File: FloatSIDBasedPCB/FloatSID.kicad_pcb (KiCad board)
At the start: 2 copper layers, 18 parts, among them M1 Motor_DC, SW1 SW, SW2 Limit Switch, U2 MS583730BA01-50, U4 XiaoESP32C3

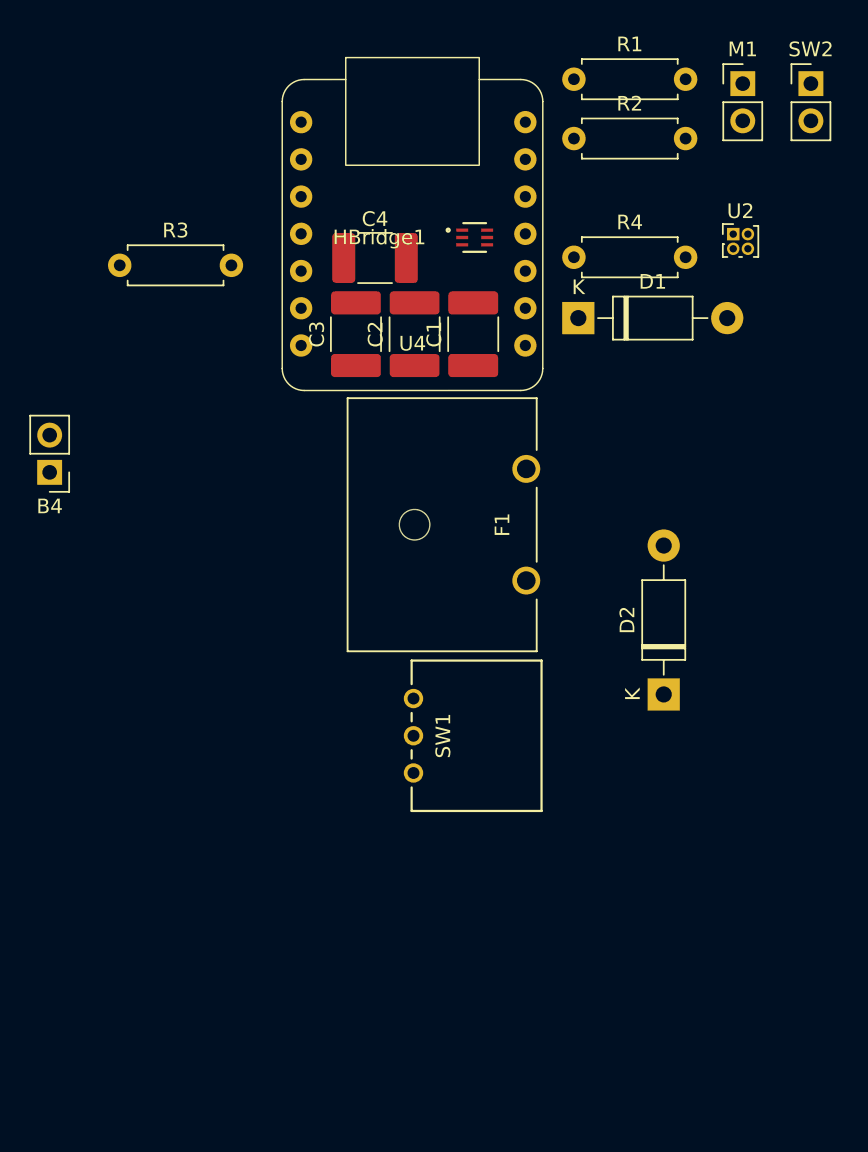
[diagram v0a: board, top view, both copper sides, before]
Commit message: Added Preliminary Traces for PCB
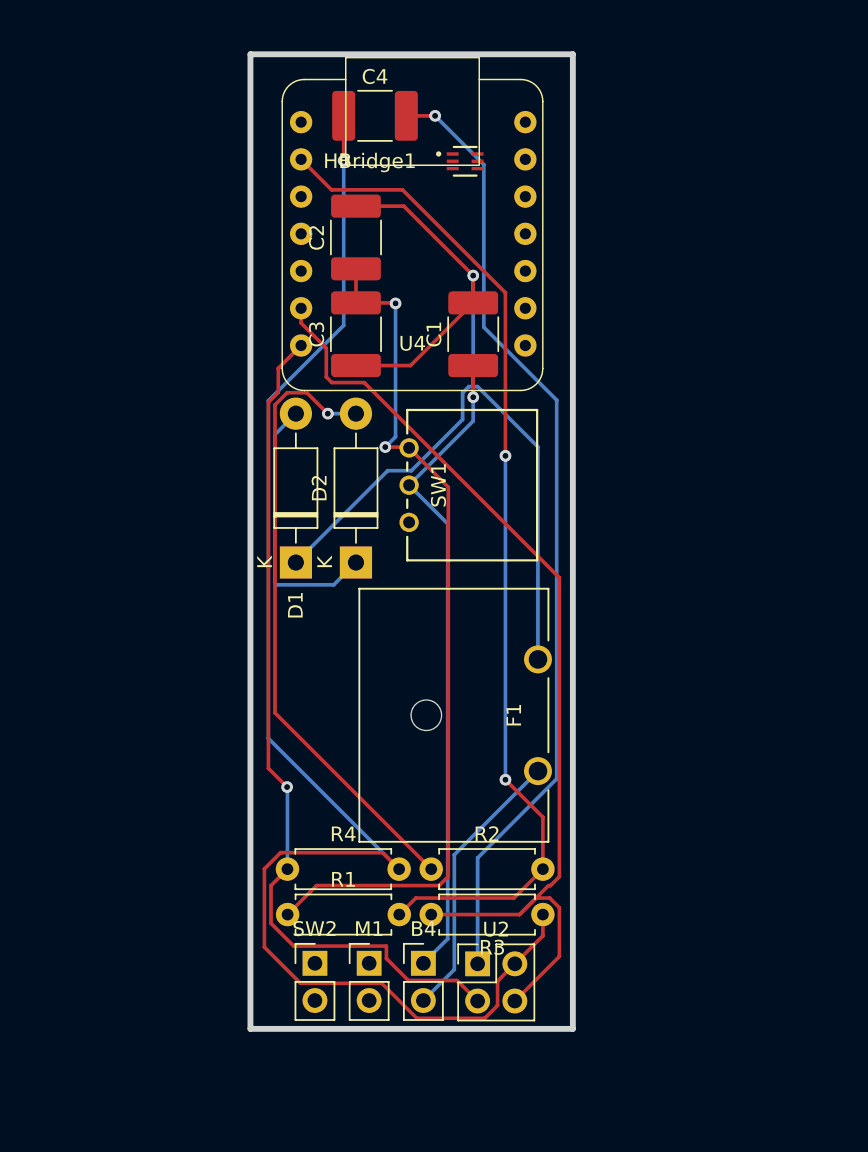
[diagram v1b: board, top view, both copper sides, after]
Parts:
- U2: footprint Connector_PinHeader_1.00mm:PinHeader_2x02_P1.00mm_Vertical -> Connector_PinHeader_2.54mm:PinHeader_2x02_P2.54mm_Vertical
- moved SW2 68.9 mm to (118.9, 135.2)
- moved M1 65.2 mm to (122.6, 135.2)
- moved R1 60.3 mm to (117.0, 131.9)
- moved R3 52.9 mm to (134.5, 131.9), turned to 180 degrees
- moved U2 52.8 mm to (130.0, 135.3)
- moved R2 50.8 mm to (126.8, 128.8)
- moved R4 46.1 mm to (117.0, 128.8)
- moved B4 42.1 mm to (126.3, 135.2), turned to 0 degrees
- moved D1 25.5 mm to (117.6, 107.9), turned to 90 degrees
- moved D2 22.8 mm to (121.7, 107.9)
- moved SW1 17.1 mm to (125.3, 102.6)
- moved F1 13.0 mm to (126.5, 118.3)
- moved C4 9.70 mm to (123.0, 77.4)
- moved C2 7.72 mm to (121.7, 85.7)
- moved HBridge1 5.24 mm to (129.1, 80.5)
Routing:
- net Net-(U2-VDD): track 0.00 -> 98.5 mm, vias 0 -> 1
- net Net-(U4-D0): track 0.00 -> 69.2 mm, vias 0 -> 2
- net Net-(U2-SDA): track 0.00 -> 68.3 mm
- net Net-(D1-K): track 0.00 -> 67.9 mm, vias 0 -> 1
- net Net-(U2-GND): track 0.00 -> 65.5 mm, vias 0 -> 1
- net Net-(HBridge1-VDD): track 0.00 -> 59.2 mm, vias 0 -> 2
- net Net-(U2-SCL): track 0.00 -> 58.2 mm, vias 0 -> 1
- net Net-(B4-+): track 0.00 -> 44.4 mm, vias 0 -> 1
- net Net-(D2-A): track 0.00 -> 43.4 mm, vias 0 -> 1
- net Net-(B4--): track 0.00 -> 18.9 mm
- net Net-(D1-A): track 0.00 -> 18.4 mm
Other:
- board outline added: 22 x 66.5 mm

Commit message: Updated PCB
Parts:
- moved H1 2.16 mm to (129.6, 82.6)
- moved C1 0.60 mm to (129.1, 92.3)
- renumbered HBridge1 to H1
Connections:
- H1 pad 1: (no net) -> Net-(HBridge1-In1)
- H1 pad 2: (no net) -> unconnected-(U4-D8-Pad9)
- H1 pad 3: (no net) -> Net-(B4--)
- H1 pad 4: (no net) -> Net-(HBridge1-Out2)
- H1 pad 5: (no net) -> Net-(B4-+)
- H1 pad 6: (no net) -> Net-(HBridge1-Out1)
- SW2 pad 1: (no net) -> unconnected-(U4-D1-Pad2)
- SW2 pad 2: (no net) -> unconnected-(U4-D2-Pad3)
- U4 pad 3V3: (no net) -> Net-(U2-VDD)
- U4 pad 4: unconnected-(U4-D3-Pad4) -> Net-(U2-SDA)
- U4 pad 5: Net-(U2-SDA) -> Net-(U2-SCL)
- U4 pad 6: Net-(U2-SCL) -> (no net)
- U4 pad GND: (no net) -> Net-(U2-GND)
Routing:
- net Net-(HBridge1-Out1): track 0.00 -> 78.2 mm, vias 0 -> 2
- net Net-(HBridge1-Out2): track 0.00 -> 70.6 mm, vias 0 -> 1
- net unconnected-(U4-D1-Pad2): track 0.00 -> 56.6 mm, vias 0 -> 2
- net unconnected-(U4-D2-Pad3): track 0.00 -> 55.2 mm, vias 0 -> 2
- net Net-(B4--): track 18.9 -> 60.1 mm
- net Net-(B4-+): track 44.4 -> 80.5 mm, vias 1 -> 3
- net Net-(U2-VDD): track 98.5 -> 121.5 mm
- net unconnected-(U4-D8-Pad9): track 0.00 -> 13.7 mm, vias 0 -> 1
- net Net-(HBridge1-In1): track 0.00 -> 13.7 mm, vias 0 -> 1
- net Net-(U2-GND): track 65.5 -> 75.0 mm
- net Net-(D1-A): track 18.4 -> 11.9 mm
- net Net-(D1-K): track 67.9 -> 73.5 mm
- net Net-(U2-SCL): track 58.2 -> 61.4 mm
- net Net-(HBridge1-VDD): track 59.2 -> 62.4 mm
- net Net-(U2-SDA): track 68.3 -> 69.5 mm
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
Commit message: Updated PCB and added Manufacturing Files
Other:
- board size 22 x 66.5 mm -> 22 x 72.8 mm
- board text added: "JLCJLCJLCJLC"
- board text added: "NanoBoard v0.0.1 S. Avetisyan"
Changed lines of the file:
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@@
       (plot_on_all_layers_selection 0x0000000_00000000)
       (disableapertmacros false)
-      (usegerberextensions false)
+      (usegerberextensions true)
       (usegerberattributes true)
       (usegerberadvancedattributes true)
-      (creategerberjobfile true)
+      (creategerberjobfile false)
       (dashed_line_dash_ratio 12.000000)
       (dashed_line_gap_ratio 3.000000)
@@
       (psa4output false)
       (plotreference true)
-      (plotvalue true)
+      (plotvalue false)
       (plotinvisibletext false)
       (sketchpadsonfab false)
-      (subtractmaskfromsilk false)
+      (subtractmaskfromsilk true)
       (outputformat 1)
       (mirror false)
-      (drillshape 1)
+      (drillshape 0)
       (scaleselection 1)
-      (outputdirectory "")
+      (outputdirectory "D:/Coding-Folder/NanoFloat/uwrov-github/nanofloat/FloatSIDBasedPCB/ManufacturingFiles/")
     )
   )
@@
     (fp_line (start 2.25 1.6) (end -2.25 1.6)
       (stroke (width 0.1) (type solid)) (layer "F.Fab"))
-    (pad "1" smd roundrect (at -2.1375 0 90) (size 1.575 3.4) (layers "F.Cu" "F.Paste" "F.Mask") (roundrect_rratio 0.15873)
+    (pad "1" smd roundrect (at -2.1375 0 90) (size 1.575 3.4) (layers "F.Cu" "F.Paste" "F.Mask") (roundrect_rratio 0.1587301587)
       (net 4 "Net-(HBridge1-VDD)") (pintype "passive"))
-    (pad "2" smd roundrect (at 2.1375 0 90) (size 1.575 3.4) (layers "F.Cu" "F.Paste" "F.Mask") (roundrect_rratio 0.15873)
+    (pad "2" smd roundrect (at 2.1375 0 90) (size 1.575 3.4) (layers "F.Cu" "F.Paste" "F.Mask") (roundrect_rratio 0.1587301587)
       (net 3 "Net-(D1-K)") (pintype "passive"))
     (model "${KICAD6_3DMODEL_DIR}/Capacitor_SMD.3dshapes/C_1812_4532Metric.wrl"
@@
     (fp_line (start 2.25 1.6) (end -2.25 1.6)
       (stroke (width 0.1) (type solid)) (layer "F.Fab"))
-    (pad "1" smd roundrect (at -2.1375 0 90) (size 1.575 3.4) (layers "F.Cu" "F.Paste" "F.Mask") (roundrect_rratio 0.15873)
+    (pad "1" smd roundrect (at -2.1375 0 90) (size 1.575 3.4) (layers "F.Cu" "F.Paste" "F.Mask") (roundrect_rratio 0.1587301587)
       (net 1 "Net-(B4-+)") (pintype "passive"))
-    (pad "2" smd roundrect (at 2.1375 0 90) (size 1.575 3.4) (layers "F.Cu" "F.Paste" "F.Mask") (roundrect_rratio 0.15873)
+    (pad "2" smd roundrect (at 2.1375 0 90) (size 1.575 3.4) (layers "F.Cu" "F.Paste" "F.Mask") (roundrect_rratio 0.1587301587)
       (net 3 "Net-(D1-K)") (pintype "passive"))
     (model "${KICAD6_3DMODEL_DIR}/Capacitor_SMD.3dshapes/C_1812_4532Metric.wrl"
@@
     (property "ki_keywords" "battery cell")
     (attr through_hole)
-    (fp_text reference "B4" (at -0.5 -2.025) (layer "F.SilkS") hide
+    (fp_text reference "B4" (at 3.3 5.175) (layer "F.SilkS")
         (effects (font (size 1 1) (thickness 0.15)))
     )
@@
     (fp_line (start 2.25 1.6) (end -2.25 1.6)
       (stroke (width 0.1) (type solid)) (layer "F.Fab"))
-    (pad "1" smd roundrect (at -2.1375 0) (size 1.575 3.4) (layers "F.Cu" "F.Paste" "F.Mask") (roundrect_rratio 0.15873)
+    (pad "1" smd roundrect (at -2.1375 0) (size 1.575 3.4) (layers "F.Cu" "F.Paste" "F.Mask") (roundrect_rratio 0.1587301587)
       (net 10 "Net-(U2-VDD)") (pintype "passive"))
-    (pad "2" smd roundrect (at 2.1375 0) (size 1.575 3.4) (layers "F.Cu" "F.Paste" "F.Mask") (roundrect_rratio 0.15873)
+    (pad "2" smd roundrect (at 2.1375 0) (size 1.575 3.4) (layers "F.Cu" "F.Paste" "F.Mask") (roundrect_rratio 0.1587301587)
       (net 14 "Net-(U2-GND)") (pintype "passive"))
     (model "${KICAD6_3DMODEL_DIR}/Capacitor_SMD.3dshapes/C_1812_4532Metric.wrl"
@@
     (property "ki_keywords" "DC Motor")
     (attr through_hole)
-    (fp_text reference "M1" (at 0 -2.33) (layer "F.SilkS") hide
+    (fp_text reference "M1" (at -0.9 5.175) (layer "F.SilkS")
         (effects (font (size 1 1) (thickness 0.15)))
     )
@@
     (fp_line (start 2.25 1.6) (end -2.25 1.6)
       (stroke (width 0.1) (type solid)) (layer "F.Fab"))
-    (pad "1" smd roundrect (at -2.1375 0 90) (size 1.575 3.4) (layers "F.Cu" "F.Paste" "F.Mask") (roundrect_rratio 0.15873)
+    (pad "1" smd roundrect (at -2.1375 0 90) (size 1.575 3.4) (layers "F.Cu" "F.Paste" "F.Mask") (roundrect_rratio 0.1587301587)
       (net 3 "Net-(D1-K)") (pintype "passive"))
-    (pad "2" smd roundrect (at 2.1375 0 90) (size 1.575 3.4) (layers "F.Cu" "F.Paste" "F.Mask") (roundrect_rratio 0.15873)
+    (pad "2" smd roundrect (at 2.1375 0 90) (size 1.575 3.4) (layers "F.Cu" "F.Paste" "F.Mask") (roundrect_rratio 0.1587301587)
       (net 4 "Net-(HBridge1-VDD)") (pintype "passive"))
     (model "${KICAD6_3DMODEL_DIR}/Capacitor_SMD.3dshapes/C_1812_4532Metric.wrl"
@@
     )
   )
-  (gr_rect (start 114.5 73.2) (end 136.5 139.7)
+  (gr_line (start 128.2 140.1) (end 127.6 139.7)
+    (stroke (width 0.15) (type default)) (layer "F.SilkS"))
+  (gr_line (start 128.6 140.1) (end 128.2 140.1)
+    (stroke (width 0.15) (type default)) (layer "F.SilkS"))
+  (gr_circle (center 125.6 142.9) (end 128.6 142.9)
+    (stroke (width 0.1) (type dot)) (fill none) (layer "Dwgs.User"))
+  (gr_rect (start 114.6 73.1) (end 136.6 145.9)
     (stroke (width 0.4) (type default)) (fill none) (layer "Edge.Cuts"))
-  (dimension (type aligned) (layer "Dwgs.User")
-    (pts (xy 114.5 73.3) (xy 136.5 73.3))
-    (height -1.1)
-    (gr_text "22.0000 mm" (at 125.5 71.05) (layer "Dwgs.User")
-      (effects (font (size 1 1) (thickness 0.15)))
-    )
-    (format (prefix "") (suffix "") (units 3) (units_format 1) (precision 4))
-    (style (thickness 0.1) (arrow_length 1.27) (text_position_mode 0) (extension_height 0.58642) (extension_offset 0.5) keep_text_aligned)
-  )
-  (dimension (type aligned) (layer "Dwgs.User")
-    (pts (xy 136.5 73.2) (xy 136.5 139.7))
-    (height -3.6)
-    (gr_text "66.5000 mm" (at 138.95 106.45 90) (layer "Dwgs.User")
-      (effects (font (size 1 1) (thickness 0.15)))
-    )
-    (format (prefix "") (suffix "") (units 3) (units_format 1) (precision 4))
-    (style (thickness 0.15) (arrow_length 1.27) (text_position_mode 0) (extension_height 0.58642) (extension_offset 0.5) keep_text_aligned)
+  (gr_circle (center 125.6 142.9) (end 127.2 142.9)
+    (stroke (width 0.15) (type default)) (fill none) (layer "Edge.Cuts"))
+  (gr_text "NanoBoard v0.0.1\nS. Avetisyan" (at 118.1 111.2 90) (layer "B.SilkS")
+    (effects (font (size 1 1) (thickness 0.15)) (justify left bottom mirror))
+  )
+  (gr_text "NanoBoard v0.0.1\nS. Avetisyan" (at 118.1 124.7 90) (layer "F.SilkS")
+    (effects (font (size 1 1) (thickness 0.15)) (justify left bottom))
+  )
+  (gr_text "JLCJLCJLCJLC" (at 123.3 111.7) (layer "F.SilkS")
+    (effects (font (size 1 1) (thickness 0.15)) (justify left bottom))
   )
   (segment (start 129.1 94.4375) (end 127.7375 95.8) (width 0.25) (layer "F.Cu") (net 1))
